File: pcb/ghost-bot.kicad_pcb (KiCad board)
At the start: 2 copper layers, 111 x 60 mm, 37 parts, among them J1 Conn_01x03_Pin, J2 Conn_01x03_Pin, J3 Conn_01x04_Pin, J4 Conn_01x02_Pin, SW1 SW_Push, SW2 SW_Push, SW3 Switch

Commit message: Add 3d model to slide switch
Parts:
- SW3: footprint Button_Switch_THT:SW_E-Switch_EG1271_SPDT -> ghost-bot-footprints:SW_E-Switch_EG1271_SPDT
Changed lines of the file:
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@@
 		)
 	)
-	(footprint "Button_Switch_THT:SW_E-Switch_EG1271_SPDT"
+	(footprint "ghost-bot-footprints:SW_E-Switch_EG1271_SPDT"
 		(layer "F.Cu")
 		(at 156.3 138.835)
@@
 			)
 		)
-		(property "Footprint" "Button_Switch_THT:SW_E-Switch_EG1271_SPDT"
+		(property "Footprint" "ghost-bot-footprints:SW_E-Switch_EG1271_SPDT"
 			(at 0 0 0)
 			(unlocked yes)
@@
 			(pintype "no_connect")
 		)
-		(model "${KICAD8_3DMODEL_DIR}/Button_Switch_THT.3dshapes/SW_E-Switch_EG1271_SPDT.wrl"
+		(model "C:/CAD/LIB_EG1271/EG1271/3D/EG1271.stp"
 			(offset
-				(xyz 0 0 0)
+				(xyz 1.55 -1.5 3.5)
 			)
 			(scale
@@
 			)
 		)
+		(sheetname "Root")
+		(sheetfile "ghost-bot.kicad_sch")
 		(attr through_hole)
 		(fp_circle
@@
 		(min_thickness 0.25)
 		(filled_areas_thickness no)
-		(fill
+		(fill yes
 			(thermal_gap 0.5)
 			(thermal_bridge_width 0.5)
@@
 		(min_thickness 0.25)
 		(filled_areas_thickness no)
-		(fill
+		(fill yes
 			(thermal_gap 0.5)
 			(thermal_bridge_width 0.5)

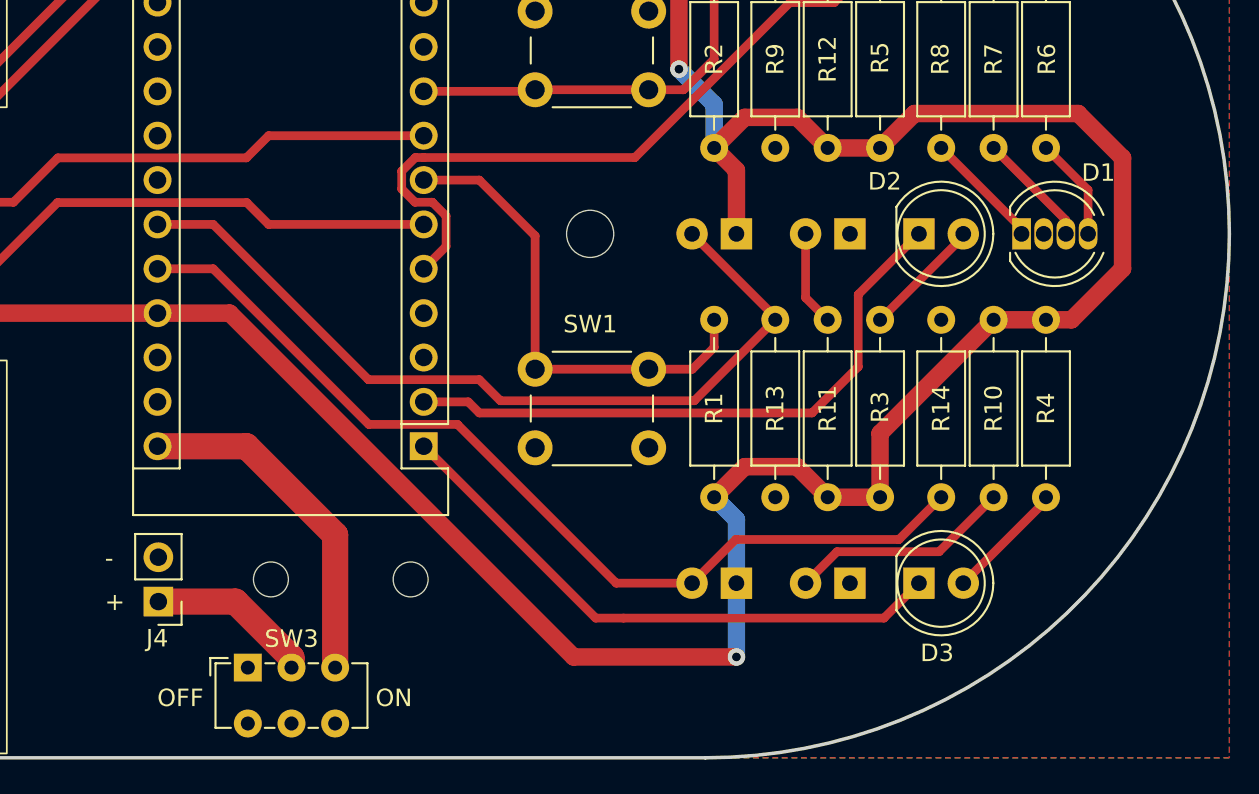
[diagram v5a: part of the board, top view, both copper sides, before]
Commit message: Replace battery connector with footprints that include strain relief, change rgb led footprint
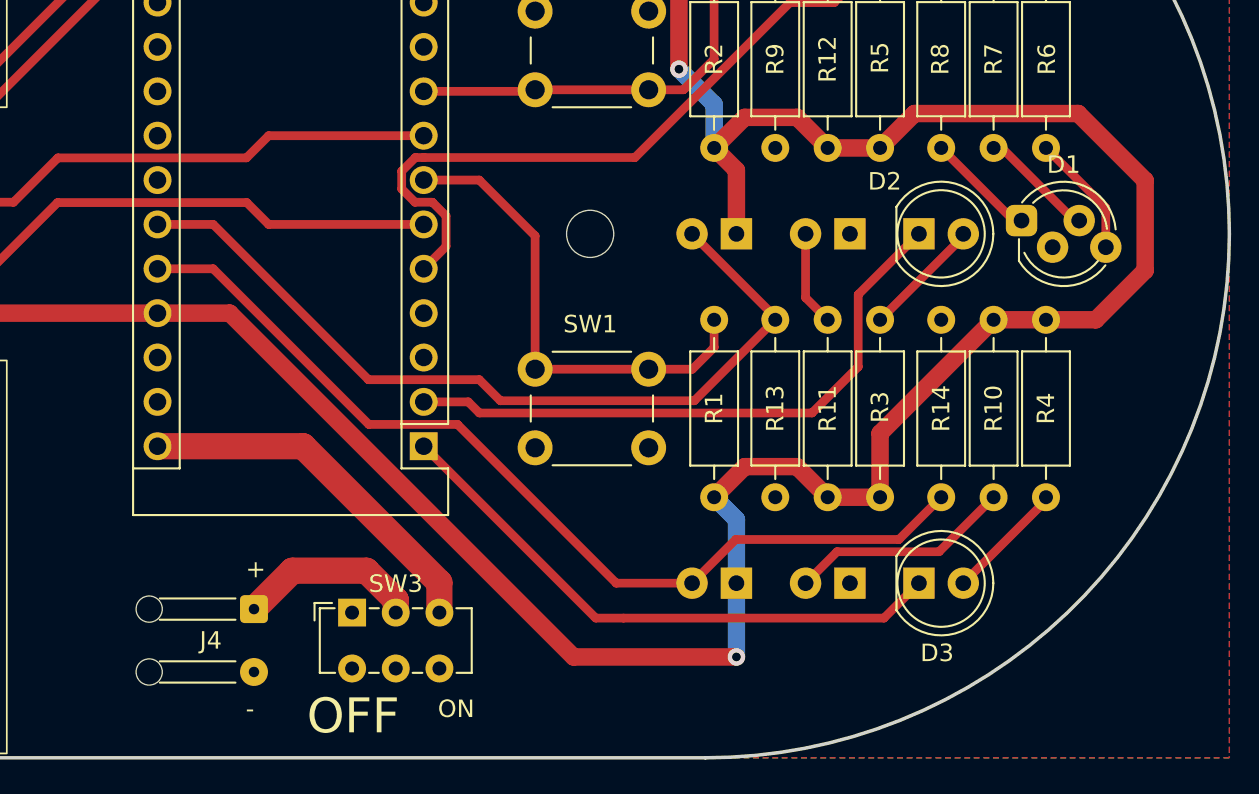
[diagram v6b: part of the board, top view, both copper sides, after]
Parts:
- removed REF** (x2): MountingHole_2.1mm, MountingHole:MountingHole_2.1mm
- D1: footprint LED_THT:LED_D5.0mm-4_RGB -> LED_THT:LED_D5.0mm-4_RGB_Staggered_Pins
- J4: footprint Connector_PinHeader_2.54mm:PinHeader_1x02_P2.54mm_Vertical -> Connector_Wire:SolderWire-0.1sqmm_1x02_P3.6mm_D0.4mm_OD1mm_Relief
- moved SW3 6.75 mm to (162.3, 135.7)
- moved J4 5.49 mm to (156.7, 135.5), turned to -90 degrees
- moved D1 0.76 mm to (200.6, 113.2)
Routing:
- net +5V: track 169.8 -> 171.7 mm
- net +BATT_SW: track 19.9 -> 21.1 mm
- net Net-(D1-RA): track 5.92 -> 7.10 mm
- net +BATT: track 9.52 -> 10.4 mm
- net Net-(D1-BA): track 6.83 -> 6.32 mm

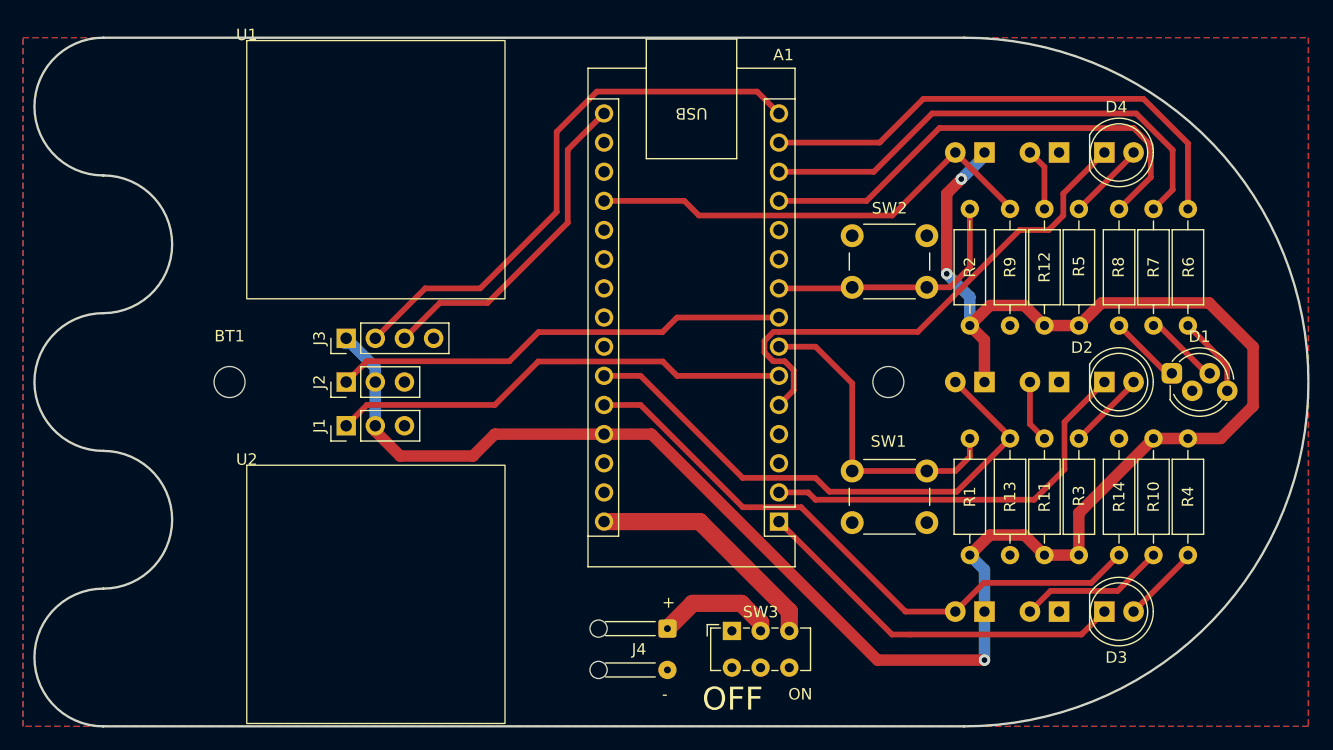
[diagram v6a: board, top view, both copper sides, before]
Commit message: Minor silkscreen changes before generating gerbers/drill
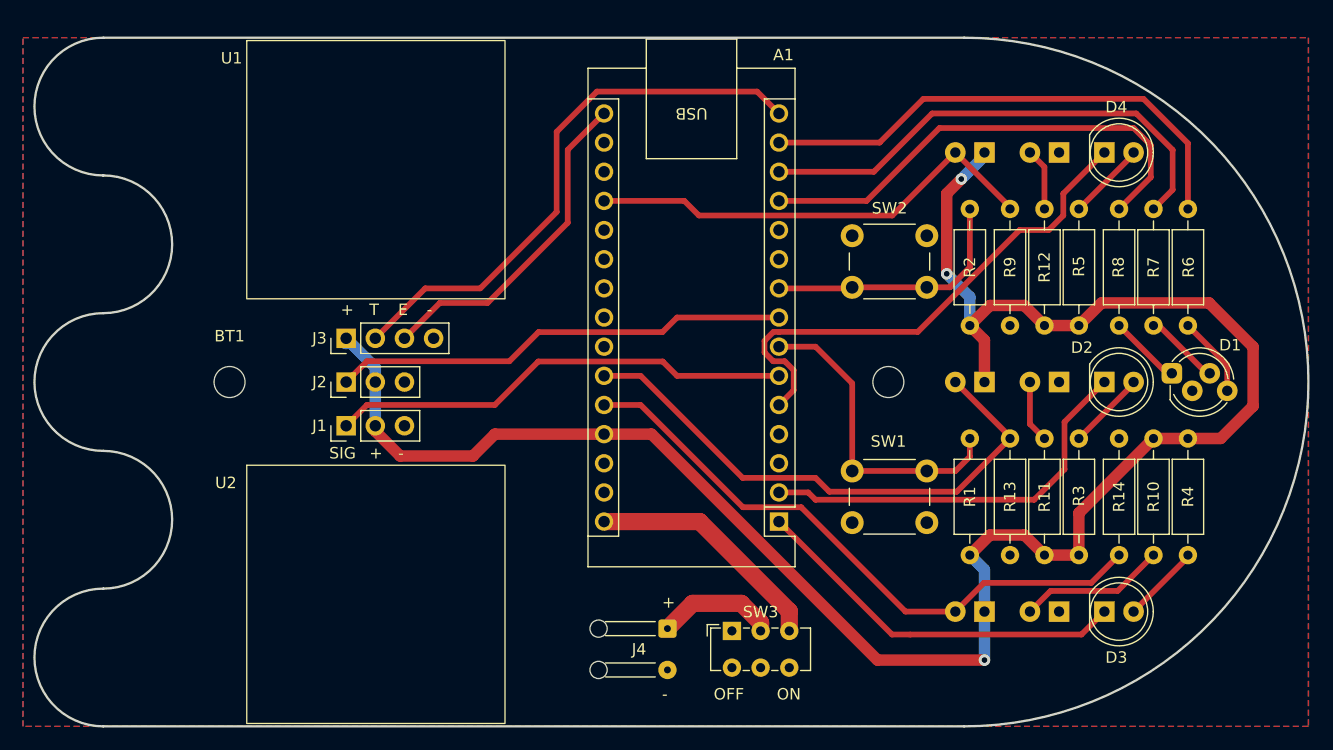
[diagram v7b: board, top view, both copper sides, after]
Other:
- board text added: "E"
- board text added: "SIG"
- board text added: "T"
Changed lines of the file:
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@@
 		(tags "Through hole pin header THT 1x03 2.54mm single row")
 		(property "Reference" "J2"
-			(at 0 -2.33 -90)
+			(at 0 -2.33 0)
 			(layer "F.SilkS")
 			(effects
@@
 		(at 120 84.25)
 		(property "Reference" "U1"
-			(at 0 -0.5 0)
+			(at -1.322857 1.534999 0)
 			(unlocked yes)
 			(layer "F.SilkS")
@@
 		(tags "rgb led")
 		(property "Reference" "D1"
-			(at 2.413 -3.198 0)
+			(at 5.07714 -2.455001 0)
 			(layer "F.SilkS")
 			(effects
@@
 		(at 120 121.25)
 		(property "Reference" "U2"
-			(at 0 -0.5 0)
+			(at -1.822857 1.534999 0)
 			(unlocked yes)
 			(layer "F.SilkS")
@@
 		(tags "Through hole pin header THT 1x04 2.54mm single row")
 		(property "Reference" "J3"
-			(at 0 -2.33 -90)
+			(at 0 -2.33 0)
 			(layer "F.SilkS")
 			(effects
@@
 		(tags "Through hole pin header THT 1x03 2.54mm single row")
 		(property "Reference" "J1"
-			(at 0 -2.33 -90)
+			(at 0 -2.33 0)
 			(layer "F.SilkS")
 			(effects
@@
 	)
 	(gr_text "OFF"
-		(at 159.677143 142.784999 0)
+		(at 160.677143 141.784999 0)
 		(layer "F.SilkS")
 		(effects
 			(font
-				(size 2 2)
-				(thickness 0.2)
+				(size 1 1)
+				(thickness 0.1)
 			)
 			(justify left bottom)
@@
 	)
 	(gr_text "ON"
-		(at 167.177143 141.784999 0)
+		(at 166.177143 141.784999 0)
 		(layer "F.SilkS")
 		(effects
@@
 		)
 	)
+	(gr_text "SIG"
+		(at 127.177143 120.784999 0)
+		(layer "F.SilkS")
+		(effects
+			(font
+				(size 1 1)
+				(thickness 0.1)
+			)
+			(justify left bottom)
+		)
+	)
+	(gr_text "T"
+		(at 130.677143 108.284999 0)
+		(layer "F.SilkS")
+		(effects
+			(font
+				(size 1 1)
+				(thickness 0.1)
+			)
+			(justify left bottom)
+		)
+	)
+	(gr_text "-"
+		(at 135.677143 108.284999 0)
+		(layer "F.SilkS")
+		(effects
+			(font
+				(size 1 1)
+				(thickness 0.1)
+			)
+			(justify left bottom)
+		)
+	)
+	(gr_text "-"
+		(at 133.177143 120.784999 0)
+		(layer "F.SilkS")
+		(effects
+			(font
+				(size 1 1)
+				(thickness 0.1)
+			)
+			(justify left bottom)
+		)
+	)
+	(gr_text "+"
+		(at 130.677143 120.784999 0)
+		(layer "F.SilkS")
+		(effects
+			(font
+				(size 1 1)
+				(thickness 0.1)
+			)
+			(justify left bottom)
+		)
+	)
 	(gr_text "+"
 		(at 156.177143 133.784999 0)
 		(layer "F.SilkS")
 		(effects
+			(font
+				(size 1 1)
+				(thickness 0.1)
+			)
+			(justify left bottom)
+		)
+	)
+	(gr_text "+"
+		(at 128.177143 108.284999 0)
+		(layer "F.SilkS")
+		(effects
+			(font
+				(size 1 1)
+				(thickness 0.1)
+			)
+			(justify left bottom)
+		)
+	)
+	(gr_text "E"
+		(at 133.177143 108.284999 0)
+		(layer "F.SilkS")
+		(effects

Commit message: Update rev to 0.1.0, update silkscreen to match and re-gen fab outputs
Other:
- board text added: "GHOST-BOT V0.1.0 0424"
- board text removed: "GHOST-BOT V0.1 0424 CK"
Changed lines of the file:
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@@
 	)
 	(paper "A4")
+	(title_block
+		(title "Ghost Bot PCB")
+		(date "2024-04-12")
+		(rev "0.1.0")
+	)
 	(layers
 		(0 "F.Cu" signal)
@@
 			(plot_on_all_layers_selection 0x0000000_00000000)
 			(disableapertmacros no)
-			(usegerberextensions no)
+			(usegerberextensions yes)
 			(usegerberattributes yes)
 			(usegerberadvancedattributes yes)
@@
 			(psa4output no)
 			(plotreference yes)
-			(plotvalue yes)
+			(plotvalue no)
 			(plotfptext yes)
 			(plotinvisibletext no)
@@
 			(outputformat 1)
 			(mirror no)
-			(drillshape 1)
+			(drillshape 0)
 			(scaleselection 1)
-			(outputdirectory "")
+			(outputdirectory "fabrication/")
 		)
 	)
@@
 		(layer "Edge.Cuts")
 	)
-	(gr_text "GHOST-BOT\nV0.1 0424 CK"
-		(at 148.185 107.81 0)
+	(gr_text "GHOST-BOT\nV0.1.0 0424"
+		(at 131.177143 107.784999 0)
 		(layer "B.SilkS" knockout)
 		(effects
@@
 				(thickness 0.3)
 			)
-			(justify left bottom mirror)
+			(justify bottom mirror)
 		)
 	)
